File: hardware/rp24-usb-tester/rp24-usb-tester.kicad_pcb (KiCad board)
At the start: 2 copper layers, 50 x 25 mm, 40 parts, among them J1 SPEAKER, J2 POWER, J3 EXT_CAP, J4 505070-2422, J5 RAILS, J6 AUX, J7 MOTOR, P1 USB_C_Receptacle_USB2.0_16P, Q1 SS8050, Q2 SS8050, Q3 SS8050, Q4 SS8050, Q5 SS8050, U1 MT2492

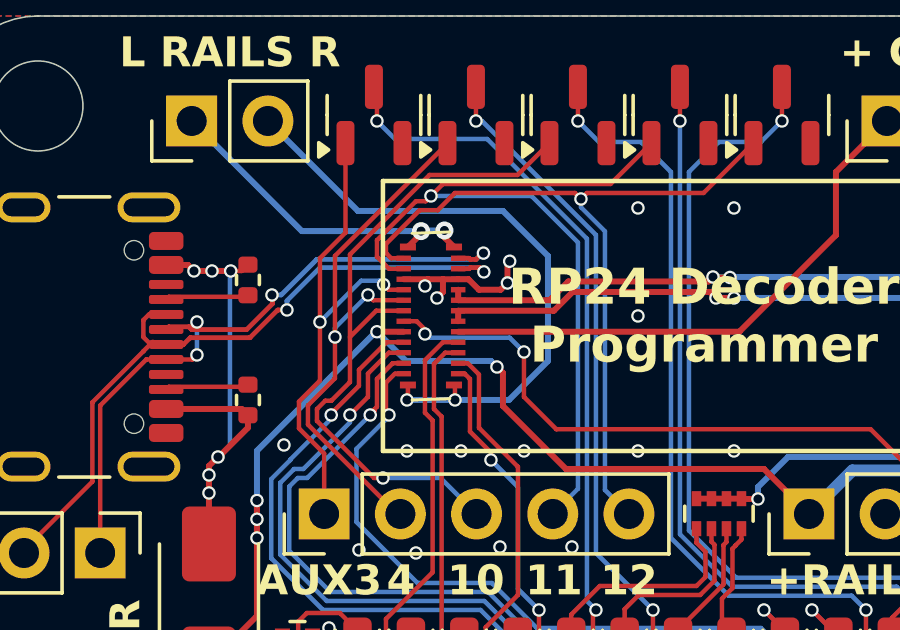
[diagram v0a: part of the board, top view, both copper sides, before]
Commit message: chore: update e24 connector model
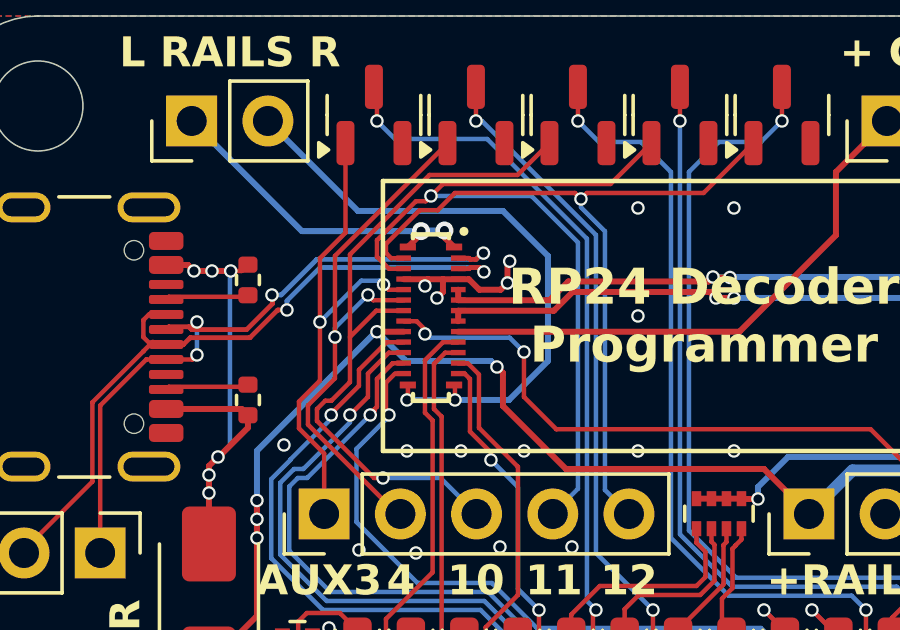
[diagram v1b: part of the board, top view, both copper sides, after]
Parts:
- J4: footprint rp24-usb-tester:5050702422 -> rp24-usb-tester:CONN-SMD_24P-P0.35_5050702422

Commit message: chore: misc cleanup
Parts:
- C1, C3: footprint rp24-usb-tester:C_0805_2012Metric -> Capacitor_SMD:C_0805_2012Metric
- C2: footprint rp24-usb-tester:C_0402_1005Metric -> Capacitor_SMD:C_0402_1005Metric
- D1, D10, D11, D12, D14, D2, D3, D4, D5, D6, D7, D8, D9: footprint rp24-usb-tester:LED_0603_1608Metric -> LED_SMD:LED_0603_1608Metric
- D13: footprint rp24-usb-tester:D_SMA -> Diode_SMD:D_SMA
- J1, J3, J5, J7: footprint rp24-usb-tester:PinHeader_1x02_P2.54mm_Vertical -> Connector_PinHeader_2.54mm:PinHeader_1x02_P2.54mm_Vertical
- J2: footprint rp24-usb-tester:PinHeader_1x04_P2.54mm_Vertical -> Connector_PinHeader_2.54mm:PinHeader_1x04_P2.54mm_Vertical
- J6: footprint rp24-usb-tester:PinHeader_1x05_P2.54mm_Vertical -> Connector_PinHeader_2.54mm:PinHeader_1x05_P2.54mm_Vertical
- P1: footprint rp24-usb-tester:USB_C_Receptacle_GCT_USB4105-xx-A_16P_TopMnt_Horizontal -> Connector_USB:USB_C_Receptacle_GCT_USB4105-xx-A_16P_TopMnt_Horizontal
- Q1, Q2, Q3, Q4, Q5: footprint rp24-usb-tester:SOT-23 -> Package_TO_SOT_SMD:SOT-23
- R1, R2, R5: footprint rp24-usb-tester:R_0402_1005Metric -> Resistor_SMD:R_0402_1005Metric
- R3, R4: footprint rp24-usb-tester:R_0603_1608Metric -> Resistor_SMD:R_0603_1608Metric
- RN1, RN2, RN3: footprint rp24-usb-tester:R_Array_Concave_4x0402 -> Resistor_SMD:R_Array_Concave_4x0402
- U1: footprint rp24-usb-tester:SOT-23-6 -> Package_TO_SOT_SMD:SOT-23-6
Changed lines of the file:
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@@
 	(net 49 "Net-(D14-K)")
 	(net 50 "Net-(U1-FB)")
-	(footprint "rp24-usb-tester:PinHeader_1x05_P2.54mm_Vertical"
+	(footprint "Connector_PinHeader_2.54mm:PinHeader_1x05_P2.54mm_Vertical"
 		(layer "F.Cu")
 		(at 138.04 116.1 90)
@@
 		)
 	)
-	(footprint "rp24-usb-tester:LED_0603_1608Metric"
+	(footprint "LED_SMD:LED_0603_1608Metric"
 		(layer "F.Cu")
 		(at 156.96296 120.775 90)
@@
 			)
 		)
-		(property "Description_1" "SlimStack Board-to-Board Connector, 0.35mm Pitch, SSB RP Series, Plug, 0.60 or 0.70mm Mated Height, 2.00mm Mated Width,  Circuits, Armor Nail, 0.15mm Fitting Nail Width"
-			(at 0 0 270)
-			(unlocked yes)
-			(layer "F.Fab")
-			(hide yes)
-			(effects
-				(font
-					(size 1 1)
-					(thickness 0.15)
-				)
-			)
-		)
-		(property "Mouser Part Number" ""
-			(at 0 0 270)
-			(unlocked yes)
-			(layer "F.Fab")
-			(hide yes)
-			(effects
-				(font
-					(size 1 1)
-					(thickness 0.15)
-				)
-			)
-		)
-		(property "Mouser Price/Stock" ""
-			(at 0 0 270)
-			(unlocked yes)
-			(layer "F.Fab")
-			(hide yes)
-			(effects
-				(font
-					(size 1 1)
-					(thickness 0.15)
-				)
-			)
-		)
 		(property "Sim.Device" ""
 			(at 0 0 270)
@@
 		)
 	)
-	(footprint "rp24-usb-tester:SOT-23"
+	(footprint "Package_TO_SOT_SMD:SOT-23"
 		(layer "F.Cu")
 		(at 139.7 102.8 90)
@@
 		)
 	)
-	(footprint "rp24-usb-tester:PinHeader_1x02_P2.54mm_Vertical"
+	(footprint "Connector_PinHeader_2.54mm:PinHeader_1x02_P2.54mm_Vertical"
 		(layer "F.Cu")
 		(at 133.625 103 90)
@@
 		)
 	)
-	(footprint "rp24-usb-tester:PinHeader_1x02_P2.54mm_Vertical"
+	(footprint "Connector_PinHeader_2.54mm:PinHeader_1x02_P2.54mm_Vertical"
 		(layer "F.Cu")
 		(at 164.325 103 90)
@@
 		)
 	)
-	(footprint "rp24-usb-tester:LED_0603_1608Metric"
+	(footprint "LED_SMD:LED_0603_1608Metric"
 		(layer "F.Cu")
 		(at 148.05648 120.775 90)
@@
 		)
 	)
-	(footprint "rp24-usb-tester:R_0603_1608Metric"
+	(footprint "Resistor_SMD:R_0603_1608Metric"
 		(layer "F.Cu")
 		(at 165.6 117.2)
@@
 		)
 	)
-	(footprint "rp24-usb-tester:R_Array_Concave_4x0402"
+	(footprint "Resistor_SMD:R_Array_Concave_4x0402"
 		(layer "F.Cu")
 		(at 137.15 120.825)
@@
 		)
 	)
-	(footprint "rp24-usb-tester:LED_0603_1608Metric"
+	(footprint "LED_SMD:LED_0603_1608Metric"
 		(layer "F.Cu")
 		(at 146.275184 120.775 90)
@@
 		)
 	)
-	(footprint "rp24-usb-tester:LED_0603_1608Metric"
+	(footprint "LED_SMD:LED_0603_1608Metric"
 		(layer "F.Cu")
 		(at 158.744256 120.775 90)
@@
 		)
 	)
-	(footprint "rp24-usb-tester:D_SMA"
+	(footprint "Diode_SMD:D_SMA"
 		(layer "F.Cu")
 		(at 134.2 119.1 90)
@@
 		)
 	)
-	(footprint "rp24-usb-tester:SOT-23"
+	(footprint "Package_TO_SOT_SMD:SOT-23"
 		(layer "F.Cu")
 		(at 149.9 102.8 90)
@@
 		)
 	)
-	(footprint "rp24-usb-tester:R_0402_1005Metric"
+	(footprint "Resistor_SMD:R_0402_1005Metric"
 		(layer "F.Cu")
 		(at 135.5 112.3 90)
@@
 		)
 	)
-	(footprint "rp24-usb-tester:SOT-23"
+	(footprint "Package_TO_SOT_SMD:SOT-23"
 		(layer "F.Cu")
 		(at 143.1 102.8 90)
@@
 		)
 	)
-	(footprint "rp24-usb-tester:SOT-23"
+	(footprint "Package_TO_SOT_SMD:SOT-23"
 		(layer "F.Cu")
 		(at 146.5 102.8 90)
@@
 		)
 	)
-	(footprint "rp24-usb-tester:LED_0603_1608Metric"
+	(footprint "LED_SMD:LED_0603_1608Metric"
 		(layer "F.Cu")
 		(at 149.837776 120.775 90)
@@
 		)
 	)
-	(footprint "rp24-usb-tester:LED_0603_1608Metric"
+	(footprint "LED_SMD:LED_0603_1608Metric"
 		(layer "F.Cu")
 		(at 139.15 120.775 90)
@@
 		)
 	)
-	(footprint "rp24-usb-tester:SOT-23-6"
+	(footprint "Package_TO_SOT_SMD:SOT-23-6"
 		(layer "F.Cu")
 		(at 166 114.5)
@@
 		)
 	)
-	(footprint "rp24-usb-tester:LED_0603_1608Metric"
+	(footprint "LED_SMD:LED_0603_1608Metric"
 		(layer "F.Cu")
 		(at 144.493888 120.775 90)
@@
 		)
 	)
-	(footprint "rp24-usb-tester:C_0805_2012Metric"
+	(footprint "Capacitor_SMD:C_0805_2012Metric"
 		(layer "F.Cu")
 		(at 165.6 107)
@@
 		)
 	)
-	(footprint "rp24-usb-tester:R_0402_1005Metric"
+	(footprint "Resistor_SMD:R_0402_1005Metric"
 		(layer "F.Cu")
 		(at 135.5 108.3 90)
@@
 		)
 	)
-	(footprint "rp24-usb-tester:PinHeader_1x02_P2.54mm_Vertical"
+	(footprint "Connector_PinHeader_2.54mm:PinHeader_1x02_P2.54mm_Vertical"
 		(layer "F.Cu")
 		(at 130.575 117.4 -90)
@@
 		)
 	)
-	(footprint "rp24-usb-tester:R_Array_Concave_4x0402"
+	(footprint "Resistor_SMD:R_Array_Concave_4x0402"
 		(layer "F.Cu")
 		(at 162.55 120.825 180)
@@
 		)
 	)
-	(footprint "rp24-usb-tester:C_0402_1005Metric"
+	(footprint "Capacitor_SMD:C_0402_1005Metric"
 		(layer "F.Cu")
 		(at 163.441172 113.316153 90)
@@
 		)
 	)
-	(footprint "rp24-usb-tester:LED_0603_1608Metric"
+	(footprint "LED_SMD:LED_0603_1608Metric"
 		(layer "F.Cu")
 		(at 140.931296 120.775 90)
@@
 		)
 	)
-	(footprint "rp24-usb-tester:USB_C_Receptacle_GCT_USB4105-xx-A_16P_TopMnt_Horizontal"
+	(footprint "Connector_USB:USB_C_Receptacle_GCT_USB4105-xx-A_16P_TopMnt_Horizontal"
 		(layer "F.Cu")
 		(at 129.095 110.2 -90)
@@
 		)
 	)
-	(footprint "rp24-usb-tester:LED_0603_1608Metric"
+	(footprint "LED_SMD:LED_0603_1608Metric"
 		(layer "F.Cu")
 		(at 142.712592 120.775 90)
@@
 		)
 	)
-	(footprint "rp24-usb-tester:PinHeader_1x02_P2.54mm_Vertical"
+	(footprint "Connector_PinHeader_2.54mm:PinHeader_1x02_P2.54mm_Vertical"
 		(layer "F.Cu")
 		(at 156.8 103 90)
@@
 		)
 	)
-	(footprint "rp24-usb-tester:SOT-23"
+	(footprint "Package_TO_SOT_SMD:SOT-23"
 		(layer "F.Cu")
 		(at 153.3 102.8 90)
@@
 		)
 	)
-	(footprint "rp24-usb-tester:LED_0603_1608Metric"
+	(footprint "LED_SMD:LED_0603_1608Metric"
 		(layer "F.Cu")
 		(at 160.525556 120.775 90)
@@
 		)
 	)
-	(footprint "rp24-usb-tester:R_0402_1005Metric"
+	(footprint "Resistor_SMD:R_0402_1005Metric"
 		(layer "F.Cu")
 		(at 164.1 121.1 90)
@@
 		)
 	)
-	(footprint "rp24-usb-tester:R_Array_Concave_4x0402"
+	(footprint "Resistor_SMD:R_Array_Concave_4x0402"
 		(layer "F.Cu")
 		(at 151.2 116.089478 -90)
@@
 		)
 	)
-	(footprint "rp24-usb-tester:C_0805_2012Metric"
+	(footprint "Capacitor_SMD:C_0805_2012Metric"
 		(layer "F.Cu")
 		(at 169.1 115.5 -90)
@@
 		)
 	)
-	(footprint "rp24-usb-tester:LED_0603_1608Metric"
+	(footprint "LED_SMD:LED_0603_1608Metric"
 		(layer "F.Cu")
 		(at 151.619072 120.775 90)
@@
 		)
 	)
-	(footprint "rp24-usb-tester:R_0603_1608Metric"
+	(footprint "Resistor_SMD:R_0603_1608Metric"
 		(layer "F.Cu")
 		(at 165.6 118.7)
@@
 		)
 	)
-	(footprint "rp24-usb-tester:LED_0603_1608Metric"
+	(footprint "LED_SMD:LED_0603_1608Metric"
 		(layer "F.Cu")
 		(at 155.181664 120.775 90)
@@
 		)
 	)
-	(footprint "rp24-usb-tester:LED_0603_1608Metric"
+	(footprint "LED_SMD:LED_0603_1608Metric"
 		(layer "F.Cu")
 		(at 153.400368 120.775 90)
@@
 		)
 	)
-	(footprint "rp24-usb-tester:PinHeader_1x04_P2.54mm_Vertical"
+	(footprint "Connector_PinHeader_2.54mm:PinHeader_1x04_P2.54mm_Vertical"
 		(layer "F.Cu")
 		(at 154.2 116.1 90)

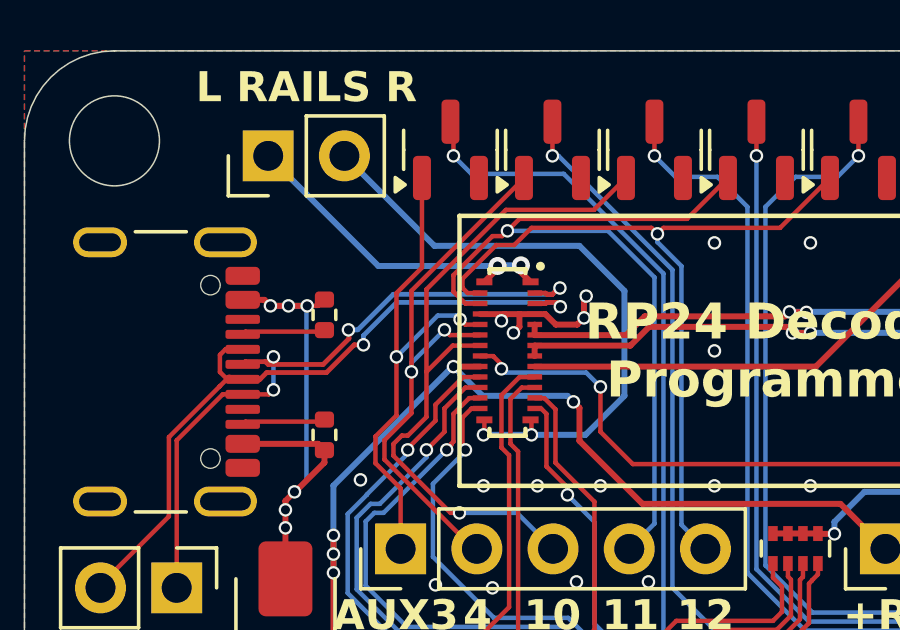
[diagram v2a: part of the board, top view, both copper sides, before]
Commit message: fix: un-swap usb +/- and aux11/aux12 pins
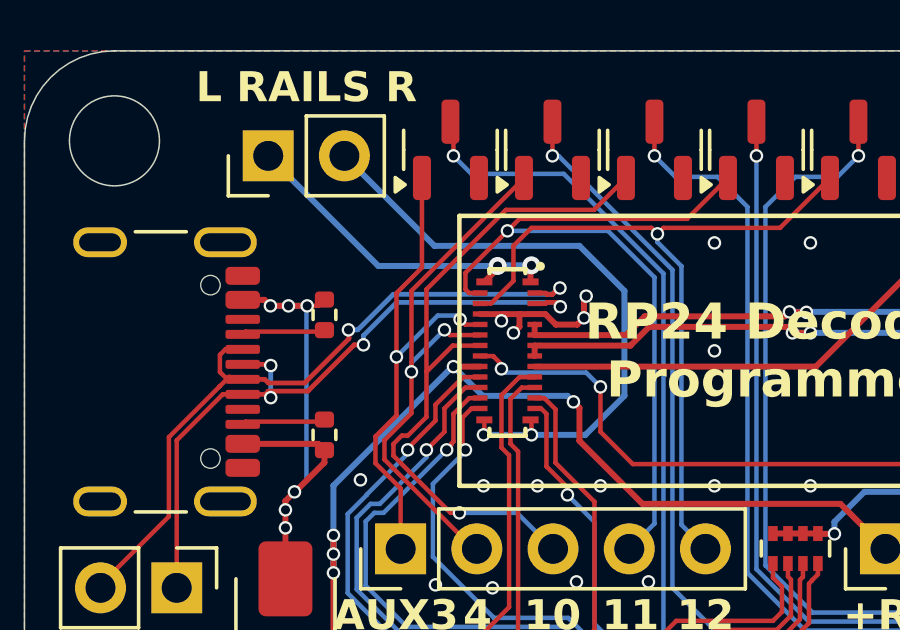
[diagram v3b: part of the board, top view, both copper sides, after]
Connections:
- J4 pad 1: /D+ -> /D-
- J4 pad 2: /D- -> /D+
- J4 pad 23: /AUX11 -> /AUX12
- J4 pad 24: /AUX12 -> /AUX11
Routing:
- net /AUX11: track 27.0 -> 26.1 mm
- net /AUX12: track 25.9 -> 25.4 mm
